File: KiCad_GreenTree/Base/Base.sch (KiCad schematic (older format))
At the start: 36 parts, among them Q1 BCX56, Q2 BCX56, Q3 BCX56, Q4 BCX56, SW1 SW_DPDT_x2, U1 NE555D, U2 NE555D, U3 74HC04, U4 L78L05_TO92

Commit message: final
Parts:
- BT3: footprint Bib:9V_Holder -> Bib:9V ohne Loecher
- C1, C10, C2, C3, C4, C5, C6, C8, C9: footprint Capacitor_SMD:C_1206_3216Metric_Pad1.33x1.80mm_HandSolder -> Capacitor_SMD:C_0805_2012Metric_Pad1.18x1.45mm_HandSolder
- R1, R3: value R -> 10k; footprint Resistor_SMD:R_1206_3216Metric_Pad1.30x1.75mm_HandSolder -> Resistor_SMD:R_0805_2012Metric_Pad1.20x1.40mm_HandSolder
- R2, R4: footprint Resistor_SMD:R_1206_3216Metric_Pad1.30x1.75mm_HandSolder -> Resistor_SMD:R_0805_2012Metric_Pad1.20x1.40mm_HandSolder
- R5, R6: value R -> 1k
- R7, R8: value R -> 1k; footprint Resistor_SMD:R_1206_3216Metric_Pad1.30x1.75mm_HandSolder -> Resistor_SMD:R_0805_2012Metric_Pad1.20x1.40mm_HandSolder
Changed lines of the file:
@@
 P 2950 1450
 F 0 "R1" H 3020 1496 50  0000 L CNN
-F 1 "R" H 3020 1405 50  0000 L CNN
-F 2 "Resistor_SMD:R_1206_3216Metric_Pad1.30x1.75mm_HandSolder" V 2880 1450 50  0001 C CNN
+F 1 "10k" H 3020 1405 50  0000 L CNN
+F 2 "Resistor_SMD:R_0805_2012Metric_Pad1.20x1.40mm_HandSolder" V 2880 1450 50  0001 C CNN
 F 3 "~" H 2950 1450 50  0001 C CNN
 	1    2950 1450
@@
 F 0 "R2" H 3020 2246 50  0000 L CNN
 F 1 "R" H 3020 2155 50  0000 L CNN
-F 2 "Resistor_SMD:R_1206_3216Metric_Pad1.30x1.75mm_HandSolder" V 2880 2200 50  0001 C CNN
+F 2 "Resistor_SMD:R_0805_2012Metric_Pad1.20x1.40mm_HandSolder" V 2880 2200 50  0001 C CNN
 F 3 "~" H 2950 2200 50  0001 C CNN
 	1    2950 2200
@@
 F 0 "C1" H 965 2346 50  0000 L CNN
 F 1 "10n" H 965 2255 50  0000 L CNN
-F 2 "Capacitor_SMD:C_1206_3216Metric_Pad1.33x1.80mm_HandSolder" H 888 2150 50  0001 C CNN
+F 2 "Capacitor_SMD:C_0805_2012Metric_Pad1.18x1.45mm_HandSolder" H 888 2150 50  0001 C CNN
 F 3 "~" H 850 2300 50  0001 C CNN
 	1    850  2300
@@
 F 0 "C3" H 3065 2646 50  0000 L CNN
 F 1 "C" H 3065 2555 50  0000 L CNN
-F 2 "Capacitor_SMD:C_1206_3216Metric_Pad1.33x1.80mm_HandSolder" H 2988 2450 50  0001 C CNN
+F 2 "Capacitor_SMD:C_0805_2012Metric_Pad1.18x1.45mm_HandSolder" H 2988 2450 50  0001 C CNN
 F 3 "~" H 2950 2600 50  0001 C CNN
 	1    2950 2600
@@
 P 2950 4300
 F 0 "R3" H 3020 4346 50  0000 L CNN
-F 1 "R" H 3020 4255 50  0000 L CNN
-F 2 "Resistor_SMD:R_1206_3216Metric_Pad1.30x1.75mm_HandSolder" V 2880 4300 50  0001 C CNN
+F 1 "10k" H 3020 4255 50  0000 L CNN
+F 2 "Resistor_SMD:R_0805_2012Metric_Pad1.20x1.40mm_HandSolder" V 2880 4300 50  0001 C CNN
 F 3 "~" H 2950 4300 50  0001 C CNN
 	1    2950 4300
@@
 F 0 "R4" H 3020 5096 50  0000 L CNN
 F 1 "R" H 3020 5005 50  0000 L CNN
-F 2 "Resistor_SMD:R_1206_3216Metric_Pad1.30x1.75mm_HandSolder" V 2880 5050 50  0001 C CNN
+F 2 "Resistor_SMD:R_0805_2012Metric_Pad1.20x1.40mm_HandSolder" V 2880 5050 50  0001 C CNN
 F 3 "~" H 2950 5050 50  0001 C CNN
 	1    2950 5050
@@
 F 0 "C2" H 965 5196 50  0000 L CNN
 F 1 "10n" H 965 5105 50  0000 L CNN
-F 2 "Capacitor_SMD:C_1206_3216Metric_Pad1.33x1.80mm_HandSolder" H 888 5000 50  0001 C CNN
+F 2 "Capacitor_SMD:C_0805_2012Metric_Pad1.18x1.45mm_HandSolder" H 888 5000 50  0001 C CNN
 F 3 "~" H 850 5150 50  0001 C CNN
 	1    850  5150
@@
 F 0 "C4" H 3065 5496 50  0000 L CNN
 F 1 "C" H 3065 5405 50  0000 L CNN
-F 2 "Capacitor_SMD:C_1206_3216Metric_Pad1.33x1.80mm_HandSolder" H 2988 5300 50  0001 C CNN
+F 2 "Capacitor_SMD:C_0805_2012Metric_Pad1.18x1.45mm_HandSolder" H 2988 5300 50  0001 C CNN
 F 3 "~" H 2950 5450 50  0001 C CNN
 	1    2950 5450
@@
 F 0 "BT3" V 9045 1100 50  0000 C CNN
 F 1 "9V" V 9136 1100 50  0000 C CNN
-F 2 "Bib:9V_Holder" V 9300 1110 50  0001 C CNN
+F 2 "Bib:9V ohne Loecher" V 9300 1110 50  0001 C CNN
 F 3 "~" V 9300 1110 50  0001 C CNN
 	1    9300 1050
@@
 P 3300 1900
 F 0 "R6" V 3093 1900 50  0000 C CNN
-F 1 "R" V 3184 1900 50  0000 C CNN
+F 1 "1k" V 3184 1900 50  0000 C CNN
 F 2 "Resistor_SMD:R_1206_3216Metric_Pad1.30x1.75mm_HandSolder" V 3230 1900 50  0001 C CNN
 F 3 "~" H 3300 1900 50  0001 C CNN
@@
 P 3250 4750
 F 0 "R5" V 3043 4750 50  0000 C CNN
-F 1 "R" V 3134 4750 50  0000 C CNN
+F 1 "1k" V 3134 4750 50  0000 C CNN
 F 2 "Resistor_SMD:R_1206_3216Metric_Pad1.30x1.75mm_HandSolder" V 3180 4750 50  0001 C CNN
 F 3 "~" H 3250 4750 50  0001 C CNN
@@
 F 0 "C6" H 2465 1346 50  0000 L CNN
 F 1 "100n" H 2465 1255 50  0000 L CNN
-F 2 "Capacitor_SMD:C_1206_3216Metric_Pad1.33x1.80mm_HandSolder" H 2388 1150 50  0001 C CNN
+F 2 "Capacitor_SMD:C_0805_2012Metric_Pad1.18x1.45mm_HandSolder" H 2388 1150 50  0001 C CNN
 F 3 "~" H 2350 1300 50  0001 C CNN
 	1    2350 1300
@@
 F 0 "C5" H 2415 4196 50  0000 L CNN
 F 1 "100n" H 2415 4105 50  0000 L CNN
-F 2 "Capacitor_SMD:C_1206_3216Metric_Pad1.33x1.80mm_HandSolder" H 2338 4000 50  0001 C CNN
+F 2 "Capacitor_SMD:C_0805_2012Metric_Pad1.18x1.45mm_HandSolder" H 2338 4000 50  0001 C CNN
 F 3 "~" H 2300 4150 50  0001 C CNN
 	1    2300 4150
@@
 F 0 "C8" H 7915 1096 50  0000 L CNN
 F 1 "100n" H 7915 1005 50  0000 L CNN
-F 2 "Capacitor_SMD:C_1206_3216Metric_Pad1.33x1.80mm_HandSolder" H 7838 900 50  0001 C CNN
+F 2 "Capacitor_SMD:C_0805_2012Metric_Pad1.18x1.45mm_HandSolder" H 7838 900 50  0001 C CNN
 F 3 "~" H 7800 1050 50  0001 C CNN
 	1    7800 1050
@@
 F 0 "C9" H 9615 2446 50  0000 L CNN
 F 1 "330n" H 9615 2355 50  0000 L CNN
-F 2 "Capacitor_SMD:C_1206_3216Metric_Pad1.33x1.80mm_HandSolder" H 9538 2250 50  0001 C CNN
+F 2 "Capacitor_SMD:C_0805_2012Metric_Pad1.18x1.45mm_HandSolder" H 9538 2250 50  0001 C CNN
 F 3 "~" H 9500 2400 50  0001 C CNN
 	1    9500 2400
@@
 F 0 "C10" H 10665 2446 50  0000 L CNN
 F 1 "10n" H 10665 2355 50  0000 L CNN
-F 2 "Capacitor_SMD:C_1206_3216Metric_Pad1.33x1.80mm_HandSolder" H 10588 2250 50  0001 C CNN
+F 2 "Capacitor_SMD:C_0805_2012Metric_Pad1.18x1.45mm_HandSolder" H 10588 2250 50  0001 C CNN
 F 3 "~" H 10550 2400 50  0001 C CNN
 	1    10550 2400
@@
 P 5450 2500
 F 0 "R8" V 5243 2500 50  0000 C CNN
-F 1 "R" V 5334 2500 50  0000 C CNN
-F 2 "Resistor_SMD:R_1206_3216Metric_Pad1.30x1.75mm_HandSolder" V 5380 2500 50  0001 C CNN
+F 1 "1k" V 5334 2500 50  0000 C CNN
+F 2 "Resistor_SMD:R_0805_2012Metric_Pad1.20x1.40mm_HandSolder" V 5380 2500 50  0001 C CNN
 F 3 "~" H 5450 2500 50  0001 C CNN
 	1    5450 2500
@@
 P 5350 5350
 F 0 "R7" V 5143 5350 50  0000 C CNN
-F 1 "R" V 5234 5350 50  0000 C CNN
-F 2 "Resistor_SMD:R_1206_3216Metric_Pad1.30x1.75mm_HandSolder" V 5280 5350 50  0001 C CNN
+F 1 "1k" V 5234 5350 50  0000 C CNN
+F 2 "Resistor_SMD:R_0805_2012Metric_Pad1.20x1.40mm_HandSolder" V 5280 5350 50  0001 C CNN
 F 3 "~" H 5350 5350 50  0001 C CNN
 	1    5350 5350

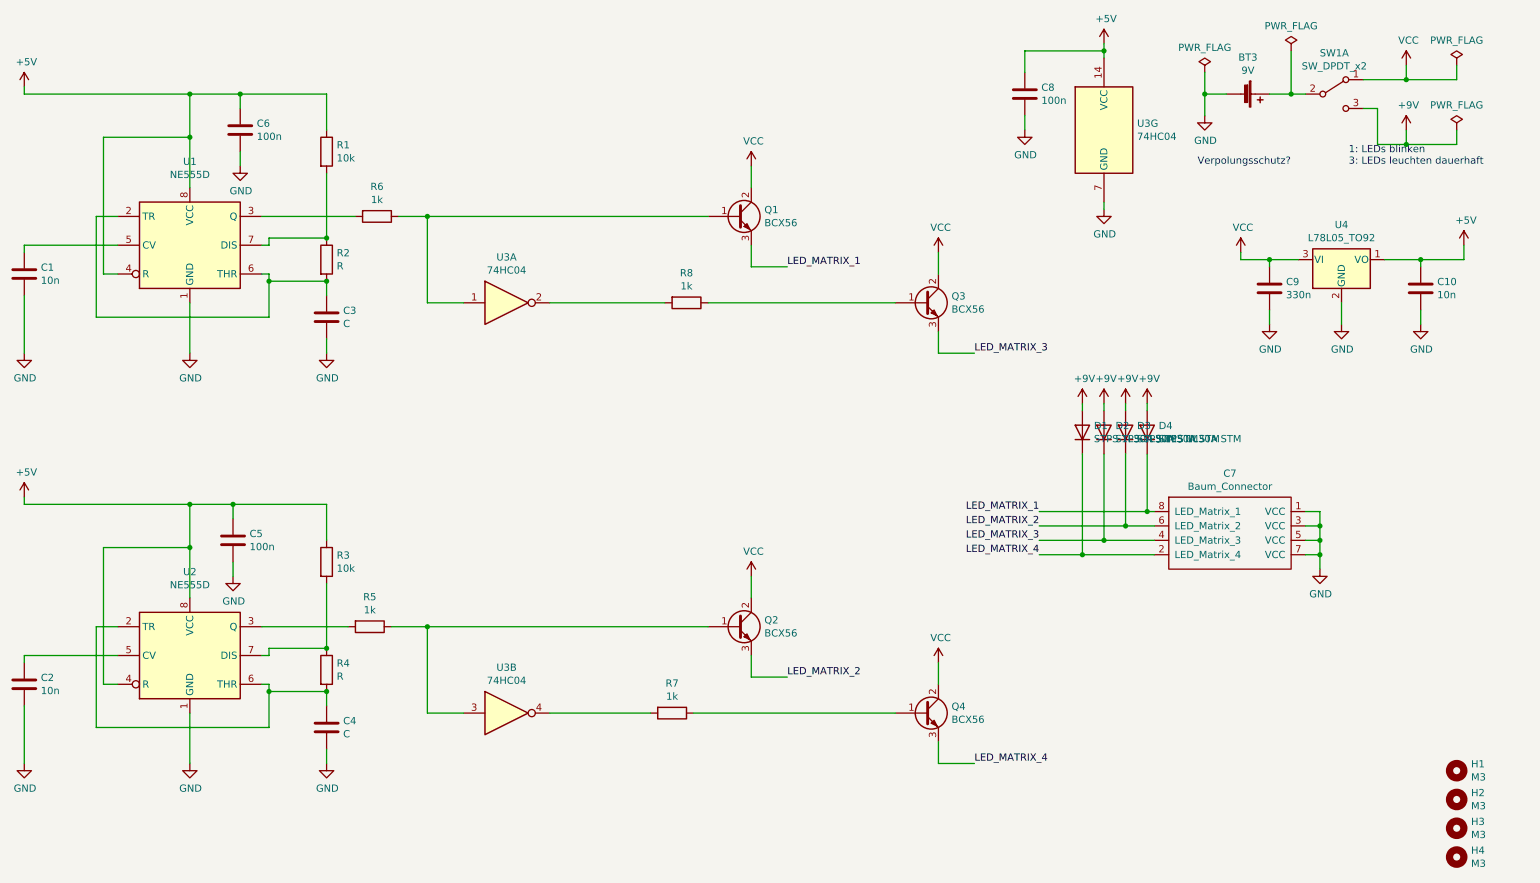
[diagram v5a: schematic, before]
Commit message: nothing works
Transistoren gegen GND schalten
Footprint Inverter und Schalter ändern
Inverter Spannungslevel anpassen. (Schalten der Transistoren beachten)
SMD linearregler?
Größere Widerstande bestellen
Andere Füße
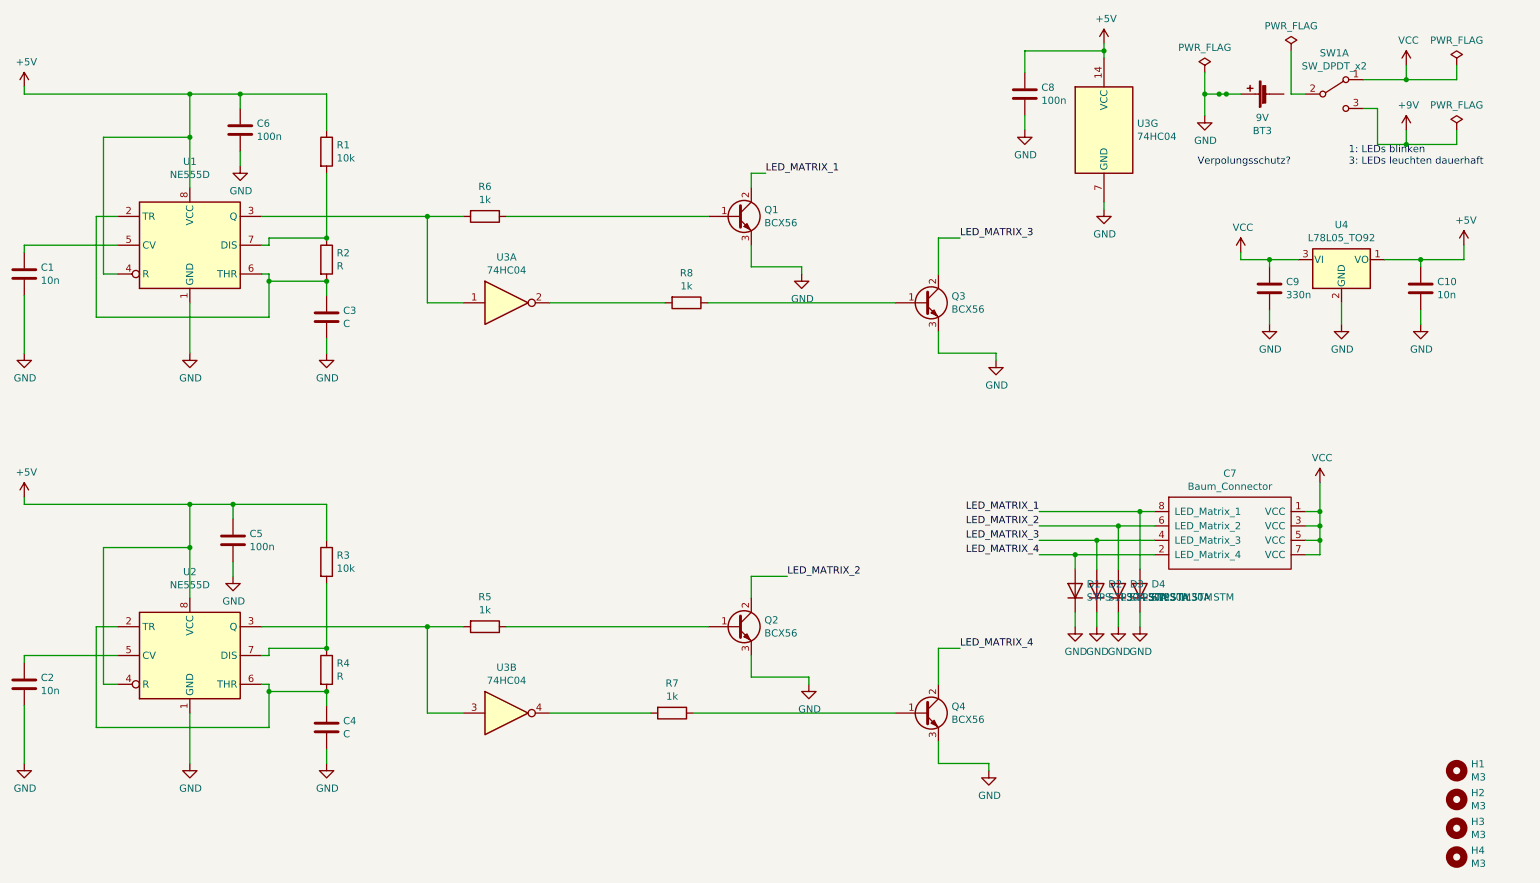
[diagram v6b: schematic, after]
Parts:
- U3: footprint Package_SO:SOIC-14W_7.5x9mm_P1.27mm -> Package_SO:SOIC-14_3.9x8.7mm_P1.27mm
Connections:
- net +9V: no longer D1.2 (A), D2.2 (A), D3.2 (A), D4.2 (A)
- net GND: now also BT3.1 (+), D1.1 (K), D2.1 (K), D3.1 (K), D4.1 (K), Q1.3 (E), Q2.3 (E), Q3.3 (E), Q4.3 (E); no longer BT3.2 (-), C7.1 (VCC), C7.3 (VCC), C7.5 (VCC), C7.7 (VCC)
- net LED_MATRIX_1: now also D4.2 (A), Q1.2 (C); no longer D4.1 (K), Q1.3 (E)
- net LED_MATRIX_2: now also D3.2 (A), Q2.2 (C); no longer D3.1 (K), Q2.3 (E)
- net LED_MATRIX_3: now also D2.2 (A), Q3.2 (C); no longer D2.1 (K), Q3.3 (E)
- net LED_MATRIX_4: now also D1.2 (A), Q4.2 (C); no longer D1.1 (K), Q4.3 (E)
- net VCC: now also C7.1 (VCC), C7.3 (VCC), C7.5 (VCC), C7.7 (VCC); no longer Q1.2 (C), Q2.2 (C), Q3.2 (C), Q4.2 (C)
- net at R6.2, U1.3 (Q): now also U3.1
- net at Q2.1 (B), R5.1: no longer U3.3
- net at R5.2, U2.3 (Q): now also U3.3
- net at SW1.2 (B): no longer BT3.1 (+)
- net at Q1.1 (B), R6.1: no longer U3.1
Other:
- moved on the sheet: BT3, D1, D2, D3, D4, R5, R6

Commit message: Base V2.0
Finished Rework. Sould now work. Hoping for the best
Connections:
- net GND: now also SW1.1 (A); no longer BT3.1 (+), D1.1 (K), D2.1 (K), D3.1 (K), D4.1 (K)
- net VCC: now also BT3.1 (+); no longer SW1.1 (A)
- net at BT3.2 (-): now also SW1.2 (B)
- net +9V renamed GND2
- net GND2: now also D1.1 (K), D2.1 (K), D3.1 (K), D4.1 (K)
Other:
- note removed: "Verpolungsschutz?"
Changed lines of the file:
@@
 	2950 5700 2950 5600
-$Comp
-L Device:Battery_Cell BT3
-U 1 1 616FC779
-P 9500 1050
-F 0 "BT3" V 9245 1100 50  0000 C CNN
-F 1 "9V" V 9336 1100 50  0000 C CNN
-F 2 "Bib:9V ohne Loecher" V 9500 1110 50  0001 C CNN
-F 3 "~" V 9500 1110 50  0001 C CNN
-	1    9500 1050
-	0    -1   -1   0
-$EndComp
-$Comp
-L power:PWR_FLAG #FLG0101
-U 1 1 61703976
-P 9650 750
-F 0 "#FLG0101" H 9650 825 50  0001 C CNN
-F 1 "PWR_FLAG" H 9650 923 50  0000 C CNN
-F 2 "" H 9650 750 50  0001 C CNN
-F 3 "~" H 9650 750 50  0001 C CNN
-	1    9650 750
-	1    0    0    -1
-$EndComp
-$Comp
-L power:PWR_FLAG #FLG0102
-U 1 1 617056E3
-P 9050 900
-F 0 "#FLG0102" H 9050 975 50  0001 C CNN
-F 1 "PWR_FLAG" H 9050 1073 50  0000 C CNN
-F 2 "" H 9050 900 50  0001 C CNN
-F 3 "~" H 9050 900 50  0001 C CNN
-	1    9050 900
-	1    0    0    -1
-$EndComp
-Wire Wire Line
-	9050 1050 9050 900
 $Comp
 L Transistor_BJT:BCX56 Q1
@@
 Wire Wire Line
 	3650 4750 3900 4750
-Wire Wire Line
-	9650 1050 9750 1050
-Wire Wire Line
-	9650 750  9650 1050
 $Comp
 L Device:R R6
@@
 	3650 5350 3900 5350
 $Comp
-L Switch:SW_DPDT_x2 SW1
-U 1 1 6176C986
-P 9950 1050
-F 0 "SW1" H 9950 1335 50  0000 C CNN
-F 1 "SW_DPDT_x2" H 9950 1244 50  0000 C CNN
-F 2 "Bib:Schiebeschalter" H 9950 1050 50  0001 C CNN
-F 3 "~" H 9950 1050 50  0001 C CNN
-	1    9950 1050
-	1    0    0    -1
-$EndComp
-$Comp
 L power:GND #PWR02
 U 1 1 61740863
@@
 Wire Wire Line
 	7200 2700 7200 2850
-$Comp
-L power:PWR_FLAG #FLG0103
-U 1 1 61739FC1
-P 10800 850
-F 0 "#FLG0103" H 10800 925 50  0001 C CNN
-F 1 "PWR_FLAG" H 10800 1023 50  0000 C CNN
-F 2 "" H 10800 850 50  0001 C CNN
-F 3 "~" H 10800 850 50  0001 C CNN
-	1    10800 850
-	1    0    0    -1
-$EndComp
-Wire Wire Line
-	10800 950  10800 850
 Wire Wire Line
 	7200 5700 7200 5550
@@
 LED_MATRIX_4
 $Comp
-L power:+9V #PWR0118
-U 1 1 617A7234
-P 10450 1300
-F 0 "#PWR0118" H 10450 1150 50  0001 C CNN
-F 1 "+9V" H 10465 1473 50  0000 C CNN
-F 2 "" H 10450 1300 50  0001 C CNN
-F 3 "" H 10450 1300 50  0001 C CNN
-	1    10450 1300
-	1    0    0    -1
-$EndComp
-$Comp
-L power:PWR_FLAG #FLG0104
-U 1 1 617A8576
-P 10800 1300
-F 0 "#FLG0104" H 10800 1375 50  0001 C CNN
-F 1 "PWR_FLAG" H 10800 1473 50  0000 C CNN
-F 2 "" H 10800 1300 50  0001 C CNN
-F 3 "~" H 10800 1300 50  0001 C CNN
-	1    10800 1300
-	1    0    0    -1
-$EndComp
-Wire Wire Line
-	10150 1150 10250 1150
-Wire Wire Line
-	10250 1150 10250 1400
-Wire Wire Line
-	10250 1400 10450 1400
-Wire Wire Line
-	10800 1400 10800 1300
-Wire Wire Line
-	10450 1300 10450 1400
-Connection ~ 10450 1400
-Wire Wire Line
-	10450 1400 10800 1400
-Text Notes 10050 1550 0    50   ~ 0
-1: LEDs blinken\n3: LEDs leuchten dauerhaft\n
-$Comp
 L power:GND #PWR0123
 U 1 1 61837F6F
@@
 	8150 4250 8700 4250
 $Comp
-L power:GND #PWR0119
-U 1 1 61A14096
+L power:GND2 #PWR0122
+U 1 1 61A1E629
+P 8600 4750
+F 0 "#PWR0122" H 8600 4500 50  0001 C CNN
+F 1 "GND2" H 8605 4577 50  0000 C CNN
+F 2 "" H 8600 4750 50  0001 C CNN
+F 3 "" H 8600 4750 50  0001 C CNN
+	1    8600 4750
+	1    0    0    -1
+$EndComp
+Wire Wire Line
+	8150 4750 8150 4650
+Wire Wire Line
+	8300 4750 8300 4650
+Wire Wire Line
+	8450 4750 8450 4650
+Wire Wire Line
+	8600 4750 8600 4650
+$Comp
+L power:GND2 #PWR0110
+U 1 1 619595BD
+P 8450 4750
+F 0 "#PWR0110" H 8450 4500 50  0001 C CNN
+F 1 "GND2" H 8455 4577 50  0000 C CNN
+F 2 "" H 8450 4750 50  0001 C CNN
+F 3 "" H 8450 4750 50  0001 C CNN
+	1    8450 4750
+	1    0    0    -1
+$EndComp
+$Comp
+L power:GND2 #PWR0118
+U 1 1 6195E8EF
+P 8300 4750
+F 0 "#PWR0118" H 8300 4500 50  0001 C CNN
+F 1 "GND2" H 8305 4577 50  0000 C CNN
+F 2 "" H 8300 4750 50  0001 C CNN
+F 3 "" H 8300 4750 50  0001 C CNN
+	1    8300 4750
+	1    0    0    -1
+$EndComp
+$Comp
+L power:GND2 #PWR0119
+U 1 1 619639EA
 P 8150 4750
 F 0 "#PWR0119" H 8150 4500 50  0001 C CNN
-F 1 "GND" H 8155 4577 50  0000 C CNN
+F 1 "GND2" H 8155 4577 50  0000 C CNN
 F 2 "" H 8150 4750 50  0001 C CNN
 F 3 "" H 8150 4750 50  0001 C CNN
@@
 	1    0    0    -1
 $EndComp
-$Comp
-L power:GND #PWR0120
-U 1 1 61A1462E
-P 8300 4750
-F 0 "#PWR0120" H 8300 4500 50  0001 C CNN
-F 1 "GND" H 8305 4577 50  0000 C CNN
-F 2 "" H 8300 4750 50  0001 C CNN
-F 3 "" H 8300 4750 50  0001 C CNN
-	1    8300 4750
-	1    0    0    -1
-$EndComp
-$Comp
-L power:GND #PWR0121
-U 1 1 61A195D5
-P 8450 4750
-F 0 "#PWR0121" H 8450 4500 50  0001 C CNN
-F 1 "GND" H 8455 4577 50  0000 C CNN
-F 2 "" H 8450 4750 50  0001 C CNN
-F 3 "" H 8450 4750 50  0001 C CNN
-	1    8450 4750
-	1    0    0    -1
-$EndComp
-$Comp
-L power:GND #PWR0122
-U 1 1 61A1E629
-P 8600 4750
-F 0 "#PWR0122" H 8600 4500 50  0001 C CNN
-F 1 "GND" H 8605 4577 50  0000 C CNN
-F 2 "" H 8600 4750 50  0001 C CNN
-F 3 "" H 8600 4750 50  0001 C CNN
-	1    8600 4750
-	1    0    0    -1
-$EndComp
-Wire Wire Line
-	8150 4750 8150 4650
-Wire Wire Line
-	8300 4750 8300 4650
-Wire Wire Line
-	8450 4750 8450 4650
-Wire Wire Line
-	8600 4750 8600 4650
-Connection ~ 10450 950
-Wire Wire Line
-	10450 950  10800 950
-Wire Wire Line
-	10150 950  10450 950
-Wire Wire Line
-	10450 950  10450 850
+Wire Wire Line
+	9050 1050 9250 1050
 $Comp
 L power:VCC #PWR0109
 U 1 1 61700D94
-P 10450 850
-F 0 "#PWR0109" H 10450 700 50  0001 C CNN
-F 1 "VCC" H 10465 1023 50  0000 C CNN
-F 2 "" H 10450 850 50  0001 C CNN
-F 3 "" H 10450 850 50  0001 C CNN
-	1    10450 850
-	1    0    0    -1
-$EndComp
+P 9250 950
+F 0 "#PWR0109" H 9250 800 50  0001 C CNN
+F 1 "VCC" H 9265 1123 50  0000 C CNN
+F 2 "" H 9250 950 50  0001 C CNN
+F 3 "" H 9250 950 50  0001 C CNN
+	1    9250 950
+	1    0    0    -1
+$EndComp
+Wire Wire Line
+	9250 1050 9250 950
 Text Notes 9000 1550 0    50   ~ 0
-Verpolungsschutz?
-Connection ~ 9200 1050
-Connection ~ 9150 1050
-Connection ~ 9050 1050
-Wire Wire Line
-	9050 1050 9300 1050
-Wire Wire Line
-	9050 1200 9050 1050
-$Comp
-L power:GND #PWR0110
-U 1 1 61701C4C
-P 9050 1200
-F 0 "#PWR0110" H 9050 950 50  0001 C CNN
-F 1 "GND" H 9055 1027 50  0000 C CNN
-F 2 "" H 9050 1200 50  0001 C CNN
-F 3 "" H 9050 1200 50  0001 C CNN
-	1    9050 1200
-	1    0    0    -1
-$EndComp
+1: LEDs blinken\n3: LEDs leuchten dauerhaft\n
+Wire Wire Line
+	10800 1400 10800 1300
+Wire Wire Line
+	10250 1150 10250 1400
+Wire Wire Line
+	10150 1150 10250 1150
+$Comp
+L power:PWR_FLAG #FLG0104
+U 1 1 617A8576
+P 10800 1300
+F 0 "#FLG0104" H 10800 1375 50  0001 C CNN
+F 1 "PWR_FLAG" H 10800 1473 50  0000 C CNN
+F 2 "" H 10800 1300 50  0001 C CNN
+F 3 "~" H 10800 1300 50  0001 C CNN
+	1    10800 1300
+	1    0    0    -1
+$EndComp
+$Comp
+L Switch:SW_DPDT_x2 SW1
+U 1 1 6176C986
+P 9950 1050
+F 0 "SW1" H 9950 1335 50  0000 C CNN
+F 1 "SW_DPDT_x2" H 9950 1244 50  0000 C CNN
+F 2 "Bib:Schiebeschalter" H 9950 1050 50  0001 C CNN
+F 3 "~" H 9950 1050 50  0001 C CNN
+	1    9950 1050
+	1    0    0    -1
+$EndComp
+Wire Wire Line
+	9650 750  9650 1050
+Wire Wire Line
+	9650 1050 9750 1050
+$Comp
+L power:PWR_FLAG #FLG0102
+U 1 1 617056E3
+P 9050 750
+F 0 "#FLG0102" H 9050 825 50  0001 C CNN
+F 1 "PWR_FLAG" H 9050 923 50  0000 C CNN
+F 2 "" H 9050 750 50  0001 C CNN
+F 3 "~" H 9050 750 50  0001 C CNN
+	1    9050 750
+	1    0    0    -1
+$EndComp
+$Comp
+L power:PWR_FLAG #FLG0101
+U 1 1 61703976
+P 9650 750
+F 0 "#FLG0101" H 9650 825 50  0001 C CNN
+F 1 "PWR_FLAG" H 9650 923 50  0000 C CNN
+F 2 "" H 9650 750 50  0001 C CNN
+F 3 "~" H 9650 750 50  0001 C CNN
+	1    9650 750
+	1    0    0    -1
+$EndComp
+$Comp
+L Device:Battery_Cell BT3
+U 1 1 616FC779
+P 9500 1050
+F 0 "BT3" V 9245 1100 50  0000 C CNN
+F 1 "9V" V 9336 1100 50  0000 C CNN
+F 2 "Bib:9V ohne Loecher" V 9500 1110 50  0001 C CNN
+F 3 "~" V 9500 1110 50  0001 C CNN
+	1    9500 1050
+	0    -1   -1   0
+$EndComp
+Wire Wire Line
+	10250 1400 10800 1400
+Connection ~ 9250 1050
+Wire Wire Line
+	9250 1050 9300 1050
+Wire Wire Line
+	9050 750  9050 1050
+$Comp
+L power:PWR_FLAG #FLG0103
+U 1 1 61739FC1
+P 10500 800
+F 0 "#FLG0103" H 10500 875 50  0001 C CNN
+F 1 "PWR_FLAG" H 10500 973 50  0000 C CNN
+F 2 "" H 10500 800 50  0001 C CNN
+F 3 "~" H 10500 800 50  0001 C CNN
+	1    10500 800
+	1    0    0    -1
+$EndComp
+$Comp
+L power:GND2 #PWR0120
+U 1 1 619A2D4A
+P 10800 1450
+F 0 "#PWR0120" H 10800 1200 50  0001 C CNN
+F 1 "GND2" H 10805 1277 50  0000 C CNN
+F 2 "" H 10800 1450 50  0001 C CNN
+F 3 "" H 10800 1450 50  0001 C CNN
+	1    10800 1450
+	1    0    0    -1
+$EndComp
+$Comp
+L power:GND #PWR0121
+U 1 1 619A843F
+P 10500 1000
+F 0 "#PWR0121" H 10500 750 50  0001 C CNN
+F 1 "GND" H 10505 827 50  0000 C CNN
+F 2 "" H 10500 1000 50  0001 C CNN
+F 3 "" H 10500 1000 50  0001 C CNN
+	1    10500 1000
+	1    0    0    -1
+$EndComp
+Wire Wire Line
+	10150 950  10500 950
+Wire Wire Line
+	10500 950  10500 1000
+Wire Wire Line
+	10500 800  10500 950
+Connection ~ 10500 950
+Wire Wire Line
+	10800 1400 10800 1450
+Connection ~ 10800 1400
+Wire Wire Line
+	9600 1050 9650 1050
+Connection ~ 9650 1050
 $EndSCHEMATC
